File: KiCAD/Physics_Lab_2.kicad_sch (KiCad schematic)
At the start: 8 parts, among them J1 USB_C, U1 MCP73871

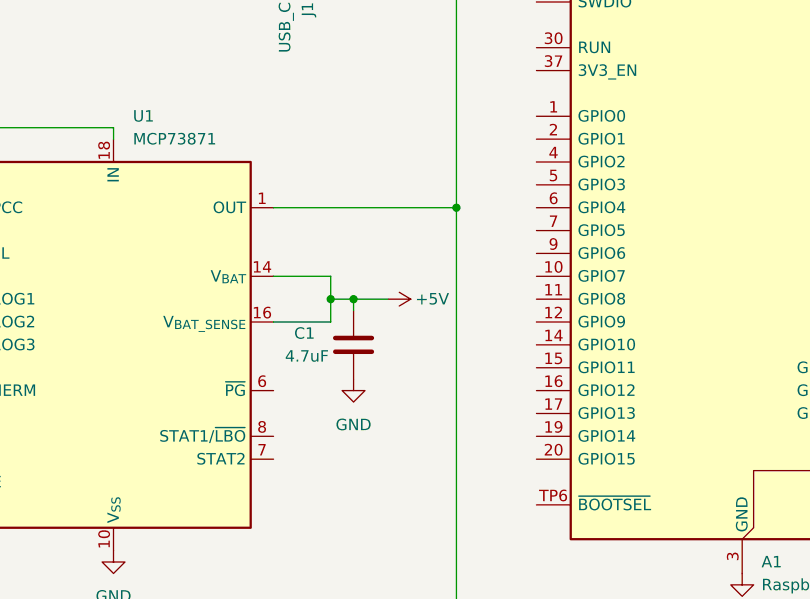
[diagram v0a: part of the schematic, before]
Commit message: Add PG and LBO connection to pico
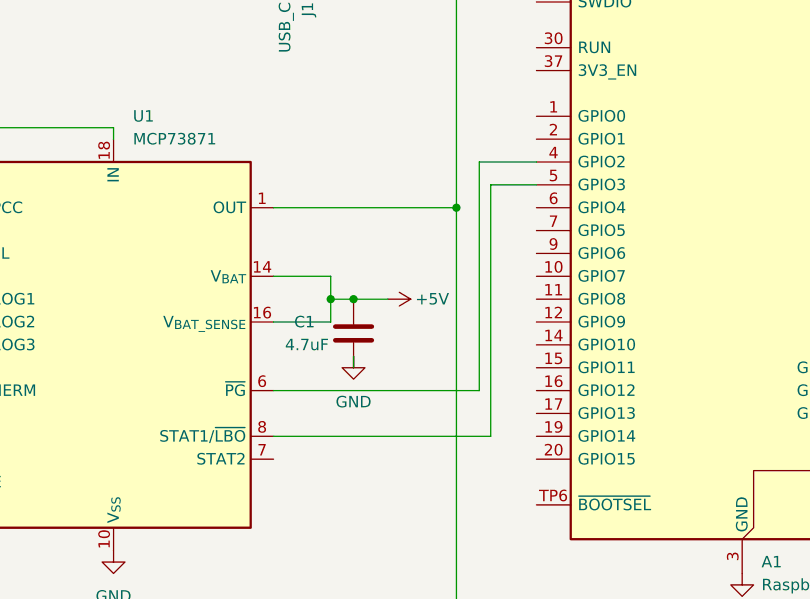
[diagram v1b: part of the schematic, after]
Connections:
- net at U1.6 (~{PG}): now also A1.4 (GPIO2)
- net at U1.8 (STAT1/~{LBO}): now also A1.5 (GPIO3)
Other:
- moved on the sheet: C1
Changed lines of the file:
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@@
 	(wire
 		(pts
-			(xy 81.28 135.89) (xy 81.28 137.16)
+			(xy 96.52 123.19) (xy 101.6 123.19)
+		)
+		(stroke
+			(width 0)
+			(type default)
+		)
+	)
+	(wire
+		(pts
+			(xy 72.39 138.43) (xy 78.74 138.43)
+		)
+		(stroke
+			(width 0)
+			(type default)
+		)
+	)
+	(wire
+		(pts
+			(xy 95.25 146.05) (xy 95.25 120.65)
+		)
+		(stroke
+			(width 0)
+			(type default)
+		)
+	)
+	(wire
+		(pts
+			(xy 163.83 135.89) (xy 163.83 176.53)
+		)
+		(stroke
+			(width 0)
+			(type default)
+		)
+	)
+	(wire
+		(pts
+			(xy 77.47 88.9) (xy 77.47 82.55)
+		)
+		(stroke
+			(width 0)
+			(type default)
+		)
+	)
+	(wire
+		(pts
+			(xy 147.32 128.27) (xy 163.83 128.27)
+		)
+		(stroke
+			(width 0)
+			(type default)
+		)
+	)
+	(wire
+		(pts
+			(xy 72.39 151.13) (xy 96.52 151.13)
+		)
+		(stroke
+			(width 0)
+			(type default)
+		)
+	)
+	(wire
+		(pts
+			(xy 54.61 116.84) (xy 54.61 118.11)
 		)
 		(stroke
@@
 	(wire
 		(pts
-			(xy 72.39 138.43) (xy 78.74 138.43)
-		)
-		(stroke
-			(width 0)
-			(type default)
-		)
-	)
-	(wire
-		(pts
-			(xy 163.83 135.89) (xy 163.83 176.53)
-		)
-		(stroke
-			(width 0)
-			(type default)
-		)
-	)
-	(wire
-		(pts
-			(xy 77.47 88.9) (xy 77.47 82.55)
-		)
-		(stroke
-			(width 0)
-			(type default)
-		)
-	)
-	(wire
-		(pts
-			(xy 147.32 128.27) (xy 163.83 128.27)
-		)
-		(stroke
-			(width 0)
-			(type default)
-		)
-	)
-	(wire
-		(pts
-			(xy 54.61 116.84) (xy 54.61 118.11)
-		)
-		(stroke
-			(width 0)
-			(type default)
-			(color 255 0 0 1)
-		)
-	)
-	(wire
-		(pts
 			(xy 78.74 135.89) (xy 81.28 135.89)
 		)
@@
 	(wire
 		(pts
+			(xy 81.28 142.24) (xy 81.28 143.51)
+		)
+		(stroke
+			(width 0)
+			(type default)
+		)
+	)
+	(wire
+		(pts
 			(xy 74.93 88.9) (xy 74.93 80.01)
 		)
@@
 	(wire
 		(pts
+			(xy 72.39 146.05) (xy 95.25 146.05)
+		)
+		(stroke
+			(width 0)
+			(type default)
+		)
+	)
+	(wire
+		(pts
 			(xy 92.71 176.53) (xy 92.71 125.73)
 		)
@@
 	(wire
 		(pts
+			(xy 96.52 151.13) (xy 96.52 123.19)
+		)
+		(stroke
+			(width 0)
+			(type default)
+		)
+	)
+	(wire
+		(pts
 			(xy 77.47 82.55) (xy 152.4 82.55)
 		)
@@
 		(pts
 			(xy 92.71 125.73) (xy 72.39 125.73)
+		)
+		(stroke
+			(width 0)
+			(type default)
+		)
+	)
+	(wire
+		(pts
+			(xy 95.25 120.65) (xy 101.6 120.65)
 		)
 		(stroke
@@
 	(symbol
 		(lib_id "power:GND")
-		(at 81.28 144.78 0)
+		(at 81.28 142.24 0)
 		(unit 1)
 		(exclude_from_sim no)
@@
 		(fields_autoplaced yes)
 		(property "Reference" "#PWR08"
-			(at 81.28 151.13 0)
+			(at 81.28 148.59 0)
 			(effects
 				(font
@@
 		)
 		(property "Value" "GND"
-			(at 81.28 149.86 0)
+			(at 81.28 147.32 0)
 			(effects
 				(font
@@
 		)
 		(property "Footprint" ""
-			(at 81.28 144.78 0)
+			(at 81.28 142.24 0)
 			(effects
 				(font
@@
 		)
 		(property "Datasheet" ""
-			(at 81.28 144.78 0)
+			(at 81.28 142.24 0)
 			(effects
 				(font
@@
 		)
 		(property "Description" "Power symbol creates a global label with name \"GND\" , ground"
-			(at 81.28 144.78 0)
+			(at 81.28 142.24 0)
 			(effects
 				(font
@@
 	(symbol
 		(lib_id "Device:C")
-		(at 81.28 140.97 0)
+		(at 81.28 139.7 0)
 		(unit 1)
 		(exclude_from_sim no)
@@
 		(dnp no)
 		(property "Reference" "C1"
-			(at 74.676 139.7 0)
+			(at 74.676 138.43 0)
 			(effects
 				(font
@@
 		)
 		(property "Value" "4.7uF"
-			(at 73.66 142.24 0)
+			(at 73.66 140.97 0)
 			(effects
 				(font
@@
 		)
 		(property "Footprint" "Capacitor_SMD:C_0805_2012Metric"
-			(at 82.2452 144.78 0)
+			(at 82.2452 143.51 0)
 			(effects
 				(font
@@
 		)
 		(property "Datasheet" "~"
-			(at 81.28 140.97 0)
+			(at 81.28 139.7 0)
 			(effects
 				(font
@@
 		)
 		(property "Description" "Unpolarized capacitor"
-			(at 81.28 140.97 0)
-			(effects
-				(font
+			(at 81.28 139.7 0)
+			(effects
+				(font
